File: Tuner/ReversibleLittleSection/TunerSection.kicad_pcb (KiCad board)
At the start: 2 copper layers, 100 x 100 mm, 123 parts, among them J1 Conn_01x03, J10 Conn_01x02, J11 Conn_02x05_Odd_Even, J12 Conn_01x01, J13 Conn_01x01, J14 Conn_01x01, J15 Conn_01x01, J16 Conn_01x01, J17 Conn_01x01, J18 Conn_01x01, J19 Conn_01x01, J2 Conn_01x03, J20 Conn_01x01, J21 Conn_01x01, J22 Conn_01x01, J23 Conn_01x02, J24 Conn_01x01, J25 Conn_01x01, J3 Conn_01x03, J4 Conn_01x03, J5 Conn_01x03, J6 Conn_01x03, J7 Conn_01x03, J8 Conn_01x02, J9 Conn_01x02, P10 Conn_01x01, P11 Conn_01x01, P12 Conn_01x01, P2 Conn_01x01, P3 Conn_01x01, P4 Conn_01x01, P5 Conn_01x01, P6 Conn_01x01, P7 Conn_01x01, P8 Conn_01x01, P9 Conn_01x01, U1 MCP23008, U2 ULN2803A

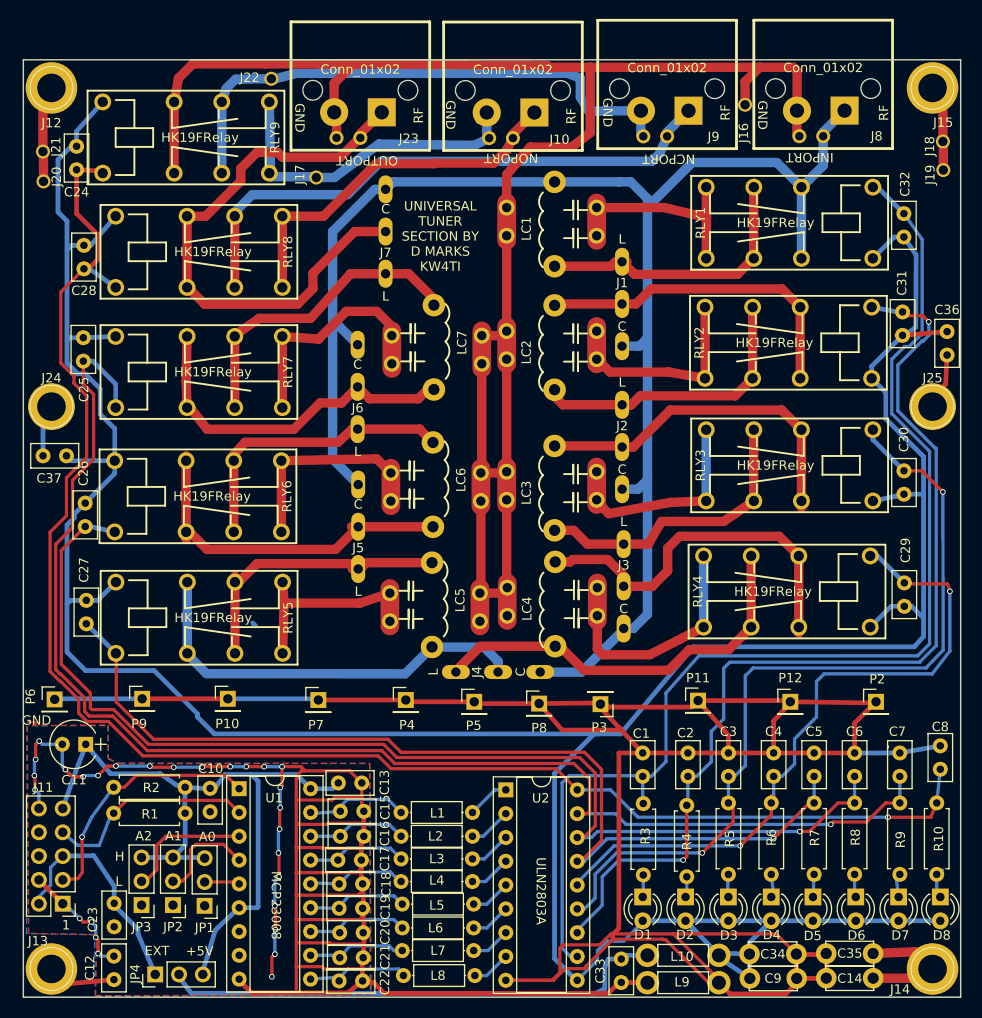
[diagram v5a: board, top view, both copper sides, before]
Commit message: Added yet more ground connections
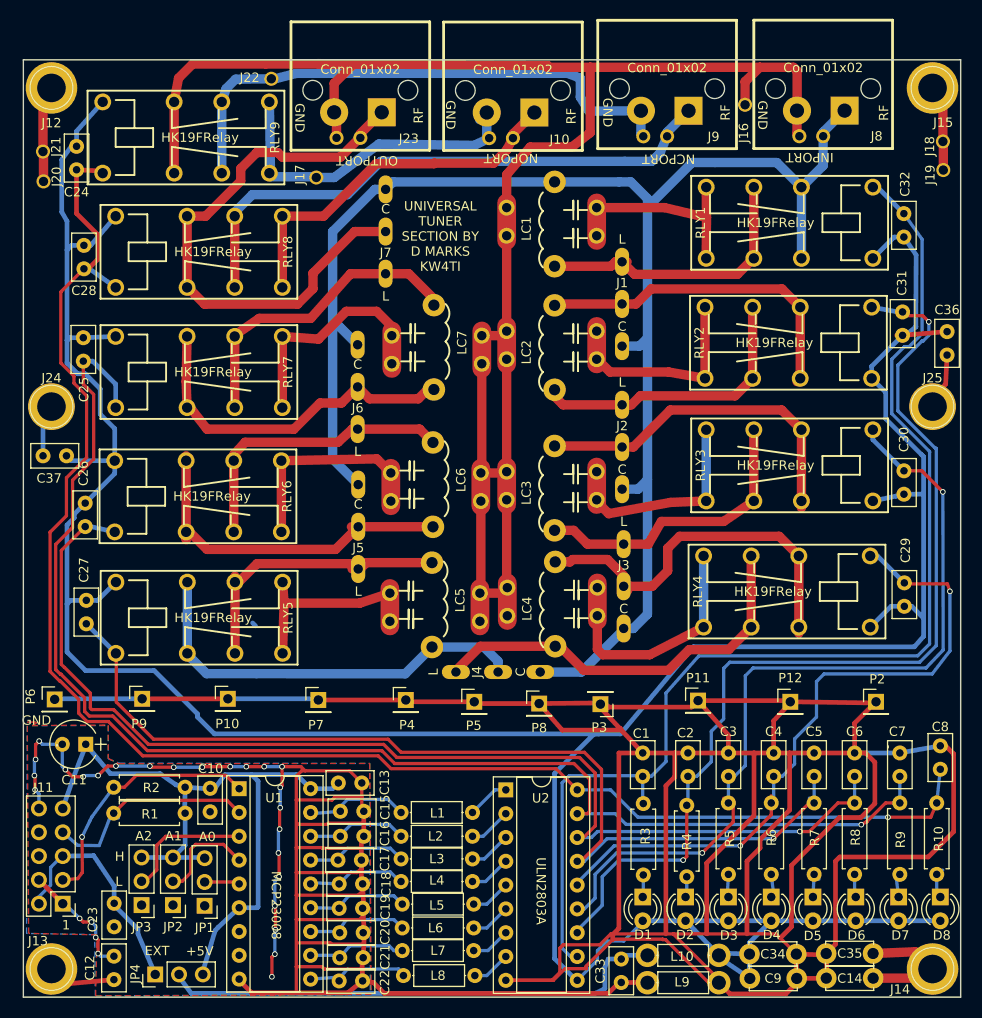
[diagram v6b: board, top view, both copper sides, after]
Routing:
- net RLYGND: track 276.0 -> 399.4 mm
- net RLYPWR: track 353.7 -> 353.2 mm
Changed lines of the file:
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@@
     (links 299)
     (no_connects 0)
-    (area 49.924999 49.924999 150.075001 150.075001)
+    (area 44.281218 45.3208 152.185 153.921938)
     (thickness 1.6)
     (drawings 30)
-    (tracks 1091)
+    (tracks 1126)
     (zones 0)
     (modules 123)
@@
   )
   (setup
-    (last_trace_width 0.25)
+    (last_trace_width 0.5)
     (user_trace_width 0.35)
     (user_trace_width 0.5)
@@
   (segment (start 141.986 129.286) (end 143.51 129.286) (width 0.35) (layer F.Cu) (net 31) (status 20))
   (segment (start 139.954 131.318) (end 141.986 129.286) (width 0.35) (layer F.Cu) (net 31))
-  (segment (start 136.398 131.318) (end 139.954 131.318) (width 0.35) (layer F.Cu) (net 31))
-  (segment (start 136.144 131.572) (end 136.398 131.318) (width 0.35) (layer F.Cu) (net 31))
-  (via (at 136.144 131.572) (size 0.6) (drill 0.4) (layers F.Cu B.Cu) (net 31))
-  (segment (start 114.3 131.572) (end 136.144 131.572) (width 0.35) (layer B.Cu) (net 31))
+  (segment (start 140.05 131.25) (end 139.954 131.318) (width 0.35) (layer F.Cu) (net 31))
+  (segment (start 139.4 131.6) (end 140.05 131.25) (width 0.35) (layer F.Cu) (net 31))
+  (via (at 139.4 131.6) (size 0.6) (drill 0.4) (layers F.Cu B.Cu) (net 31))
+  (segment (start 114.3 131.572) (end 139.4 131.6) (width 0.35) (layer B.Cu) (net 31))
   (segment (start 113.157 130.429) (end 114.3 131.572) (width 0.35) (layer B.Cu) (net 31))
   (segment (start 143.51 126.452) (end 143.51 129.286) (width 0.35) (layer B.Cu) (net 31) (status 30))
@@
   (segment (start 148.463 138.684) (end 147.828 139.319) (width 0.35) (layer B.Cu) (net 46) (status 30))
   (segment (start 147.9296 136.6012) (end 148.082 136.4488) (width 0.35) (layer B.Cu) (net 46) (status 30))
+  (segment (start 138.684 123.952) (end 139.852 123.952) (width 0.5) (layer F.Cu) (net 47))
+  (segment (start 131.95 142.5) (end 130.75372 143.69628) (width 0.5) (layer F.Cu) (net 47))
+  (segment (start 131.95 135.95) (end 131.95 142.5) (width 0.5) (layer F.Cu) (net 47))
+  (segment (start 137.05 130.85) (end 131.95 135.95) (width 0.5) (layer F.Cu) (net 47))
+  (segment (start 139.35 130.85) (end 137.05 130.85) (width 0.5) (layer F.Cu) (net 47))
+  (segment (start 140.85 129.35) (end 139.35 130.85) (width 0.5) (layer F.Cu) (net 47))
+  (segment (start 140.85 124.95) (end 140.85 129.35) (width 0.5) (layer F.Cu) (net 47))
+  (segment (start 139.852 123.952) (end 140.85 124.95) (width 0.5) (layer F.Cu) (net 47))
+  (segment (start 127.95 123.952) (end 127.95 130.65) (width 0.5) (layer F.Cu) (net 47))
+  (segment (start 122.9 143.2) (end 122.956 143.256) (width 0.5) (layer F.Cu) (net 47))
+  (segment (start 122.9 135.7) (end 122.9 143.2) (width 0.5) (layer F.Cu) (net 47))
+  (segment (start 127.95 130.65) (end 122.9 135.7) (width 0.5) (layer F.Cu) (net 47))
+  (segment (start 131.75 123.952) (end 131.75 130.05) (width 0.5) (layer F.Cu) (net 47))
+  (segment (start 127.2 135.5) (end 127.2 143.256) (width 0.5) (layer F.Cu) (net 47))
+  (segment (start 128.6 134.1) (end 127.2 135.5) (width 0.5) (layer F.Cu) (net 47))
+  (segment (start 128.6 133.2) (end 128.6 134.1) (width 0.5) (layer F.Cu) (net 47))
+  (segment (start 131.75 130.05) (end 128.6 133.2) (width 0.5) (layer F.Cu) (net 47))
+  (segment (start 119.5 123.952) (end 119.5 126.5) (width 0.5) (layer F.Cu) (net 47))
+  (segment (start 118.55 127.45) (end 118.55 143.256) (width 0.5) (layer F.Cu) (net 47))
+  (segment (start 119.5 126.5) (end 118.55 127.45) (width 0.5) (layer F.Cu) (net 47))
+  (segment (start 147.828 123.19) (end 148.39 123.19) (width 0.5) (layer F.Cu) (net 47))
+  (segment (start 148.39 123.19) (end 149.25 124.05) (width 0.5) (layer F.Cu) (net 47))
+  (segment (start 136.65 144.354) (end 135.65504 145.34896) (width 0.5) (layer F.Cu) (net 47))
+  (segment (start 136.65 135.5) (end 136.65 144.354) (width 0.5) (layer F.Cu) (net 47))
+  (segment (start 137.1 135.05) (end 136.65 135.5) (width 0.5) (layer F.Cu) (net 47))
+  (segment (start 146.55 135.05) (end 137.1 135.05) (width 0.5) (layer F.Cu) (net 47))
+  (segment (start 149.25 132.35) (end 146.55 135.05) (width 0.5) (layer F.Cu) (net 47))
+  (segment (start 149.25 124.05) (end 149.25 132.35) (width 0.5) (layer F.Cu) (net 47))
   (segment (start 107.483785 121.511322) (end 113.797893 121.511322) (width 0.5) (layer F.Cu) (net 47))
   (segment (start 113.665 121.3104) (end 113.665 121.36907) (width 0.5) (layer F.Cu) (net 47))
@@
   (segment (start 105.029 118.6815) (end 98.298 118.6815) (width 0.5) (layer F.Cu) (net 47) (status 30))
   (segment (start 98.298 118.6815) (end 98.1075 118.491) (width 0.5) (layer F.Cu) (net 47) (status 30))
-  (segment (start 119.3292 143.256) (end 130.31344 143.256) (width 0.35) (layer F.Cu) (net 47))
-  (segment (start 130.31344 143.256) (end 132.46736 145.40992) (width 0.35) (layer F.Cu) (net 47) (status 20))
+  (segment (start 119.3292 143.256) (end 122.956 143.256) (width 0.35) (layer F.Cu) (net 47))
+  (segment (start 122.956 143.256) (end 127.2 143.256) (width 0.35) (layer F.Cu) (net 47))
+  (segment (start 127.2 143.256) (end 130.31344 143.256) (width 0.35) (layer F.Cu) (net 47))
+  (segment (start 130.31344 143.256) (end 130.75372 143.69628) (width 0.35) (layer F.Cu) (net 47) (status 20))
+  (segment (start 130.75372 143.69628) (end 132.46736 145.40992) (width 0.35) (layer F.Cu) (net 47) (status 20))
   (segment (start 118.2116 143.8656) (end 118.5164 143.8656) (width 0.35) (layer F.Cu) (net 47))
   (segment (start 118.5164 143.8656) (end 123.1138 148.463) (width 0.35) (layer F.Cu) (net 47) (status 20))
@@
   (segment (start 118.2116 143.8148) (end 118.2116 143.8656) (width 0.35) (layer F.Cu) (net 47))
   (segment (start 101.473 148.209) (end 106.4006 148.209) (width 0.35) (layer F.Cu) (net 47) (status 10))
-  (segment (start 119.3292 143.256) (end 124.206 148.1328) (width 0.35) (layer F.Cu) (net 47) (status 20))
-  (segment (start 112.6744 143.256) (end 119.3292 143.256) (width 0.35) (layer F.Cu) (net 47))
-  (segment (start 111.506 144.4244) (end 112.6744 143.256) (width 0.35) (layer F.Cu) (net 47))
-  (segment (start 107.5944 144.4244) (end 111.506 144.4244) (width 0.35) (layer F.Cu) (net 47))
-  (segment (start 107.2388 144.78) (end 107.5944 144.4244) (width 0.35) (layer F.Cu) (net 47))
-  (segment (start 107.2388 147.3708) (end 107.2388 144.78) (width 0.35) (layer F.Cu) (net 47))
   (segment (start 106.4006 148.209) (end 107.2388 147.3708) (width 0.35) (layer F.Cu) (net 47))
+  (segment (start 107.2388 147.3708) (end 107.2388 144.78) (width 0.35) (layer F.Cu) (net 47))
+  (segment (start 107.2388 144.78) (end 107.5944 144.4244) (width 0.35) (layer F.Cu) (net 47))
+  (segment (start 107.5944 144.4244) (end 111.506 144.4244) (width 0.35) (layer F.Cu) (net 47))
+  (segment (start 111.506 144.4244) (end 112.6744 143.256) (width 0.35) (layer F.Cu) (net 47))
+  (segment (start 112.6744 143.256) (end 118.55 143.256) (width 0.35) (layer F.Cu) (net 47))
+  (segment (start 119.3292 143.256) (end 124.206 148.1328) (width 0.35) (layer F.Cu) (net 47) (status 20))
+  (segment (start 118.55 143.256) (end 119.3292 143.256) (width 0.35) (layer F.Cu) (net 47))
   (segment (start 124.206 148.1328) (end 124.206 148.463) (width 0.35) (layer F.Cu) (net 47) (status 30))
   (segment (start 135.65504 145.34896) (end 135.7414 147.9042) (width 0.5) (layer F.Cu) (net 47) (status 30))
@@
   (segment (start 143.51 123.952) (end 138.684 123.952) (width 0.5) (layer B.Cu) (net 47) (status 30))
   (segment (start 134.366 123.952) (end 138.684 123.952) (width 0.5) (layer F.Cu) (net 47) (status 30))
-  (segment (start 130.048 123.952) (end 134.366 123.952) (width 0.5) (layer F.Cu) (net 47) (status 30))
-  (segment (start 125.222 123.952) (end 130.048 123.952) (width 0.5) (layer F.Cu) (net 47) (status 30))
+  (segment (start 130.048 123.952) (end 131.75 123.952) (width 0.5) (layer F.Cu) (net 47) (status 30))
+  (segment (start 131.75 123.952) (end 134.366 123.952) (width 0.5) (layer F.Cu) (net 47) (status 30))
+  (segment (start 125.222 123.952) (end 127.95 123.952) (width 0.5) (layer F.Cu) (net 47) (status 30))
+  (segment (start 127.95 123.952) (end 130.048 123.952) (width 0.5) (layer F.Cu) (net 47) (status 30))
   (segment (start 120.904 123.952) (end 125.222 123.952) (width 0.5) (layer F.Cu) (net 47) (status 30))
-  (segment (start 116.078 123.952) (end 120.904 123.952) (width 0.5) (layer F.Cu) (net 47) (status 30))
+  (segment (start 116.078 123.952) (end 119.5 123.952) (width 0.5) (layer F.Cu) (net 47) (status 30))
+  (segment (start 119.5 123.952) (end 120.904 123.952) (width 0.5) (layer F.Cu) (net 47) (status 30))
   (segment (start 116.078 123.952) (end 113.538 123.952) (width 0.5) (layer F.Cu) (net 47) (status 10))
   (segment (start 101.6 148.082) (end 101.473 148.209) (width 0.5) (layer F.Cu) (net 47) (status 30))
@@
   (segment (start 55.6768 57.6248) (end 58.46824 54.493) (width 0.5) (layer B.Cu) (net 48) (status 20))
   (segment (start 55.6768 59.2328) (end 55.118 59.2328) (width 0.5) (layer B.Cu) (net 48))
-  (segment (start 55.118 59.2328) (end 53.6956 60.6552) (width 0.5) (layer B.Cu) (net 48))
-  (segment (start 53.6956 60.6552) (end 53.6956 66.2432) (width 0.5) (layer B.Cu) (net 48))
-  (segment (start 53.6956 66.2432) (end 54.6608 67.2084) (width 0.5) (layer B.Cu) (net 48))
+  (segment (start 55.118 59.2328) (end 54.0996 60.6552) (width 0.5) (layer B.Cu) (net 48))
+  (segment (start 54.0996 60.6552) (end 54.0996 66.2432) (width 0.5) (layer B.Cu) (net 48))
+  (segment (start 54.0996 66.2432) (end 54.6608 67.2084) (width 0.5) (layer B.Cu) (net 48))
   (segment (start 56.4642 69.7992) (end 57.193 69.7992) (width 0.5) (layer B.Cu) (net 48))
   (segment (start 57.193 69.7992) (end 59.85 66.685) (width 0.5) (layer B.Cu) (net 48) (status 20))
